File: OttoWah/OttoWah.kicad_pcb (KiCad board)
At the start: 2 copper layers, 38.6 x 34.5 mm, 26 parts, among them J1 Conn_01x02_Female, J2 Conn_01x02_Female, J3 Conn_01x01_Female, J4 Conn_01x01_Female, J5 Conn_01x01_Female, J6 Conn_01x01_Female, U1 TL072, U2 Optocoupler

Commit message: First revision of pedal board - all footprints finalized
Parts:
- moved J4 34.7 mm to (190.2, 55.3)
- moved R3 18.8 mm to (172.8, 65.0), turned to 180 degrees
- moved D1 7.15 mm to (188.0, 37.5)
- moved U2 6.11 mm to (157.5, 34.3)
- moved C1 4.96 mm to (165.1, 60.3), turned to 270 degrees
- moved J1 2.67 mm to (161.3, 64.1), turned to 180 degrees
- moved R8 0.89 mm to (177.8, 42.9)
- moved R5 0.76 mm to (157.5, 43.9)
- moved R1 0.16 mm to (167.7, 60.3)
- moved R2 0.16 mm to (167.7, 62.6)
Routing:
- net Net-(R3-Pad1): track 12.6 -> 51.4 mm
- net Net-(C1-Pad1): track 31.8 -> 22.6 mm
- net Net-(D1-Pad2): track 6.44 -> 11.4 mm
- net Net-(C2-Pad2): track 25.1 -> 29.5 mm
- net Net-(R2-Pad1): track 15.8 -> 16.6 mm
- net Net-(R5-Pad1): track 9.14 -> 8.57 mm
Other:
- net class Default: trace_width 0.25 -> 0.254
- net class Power added: clearance 0.2, trace_width 0.508, via_dia 0.8, via_drill 0.4

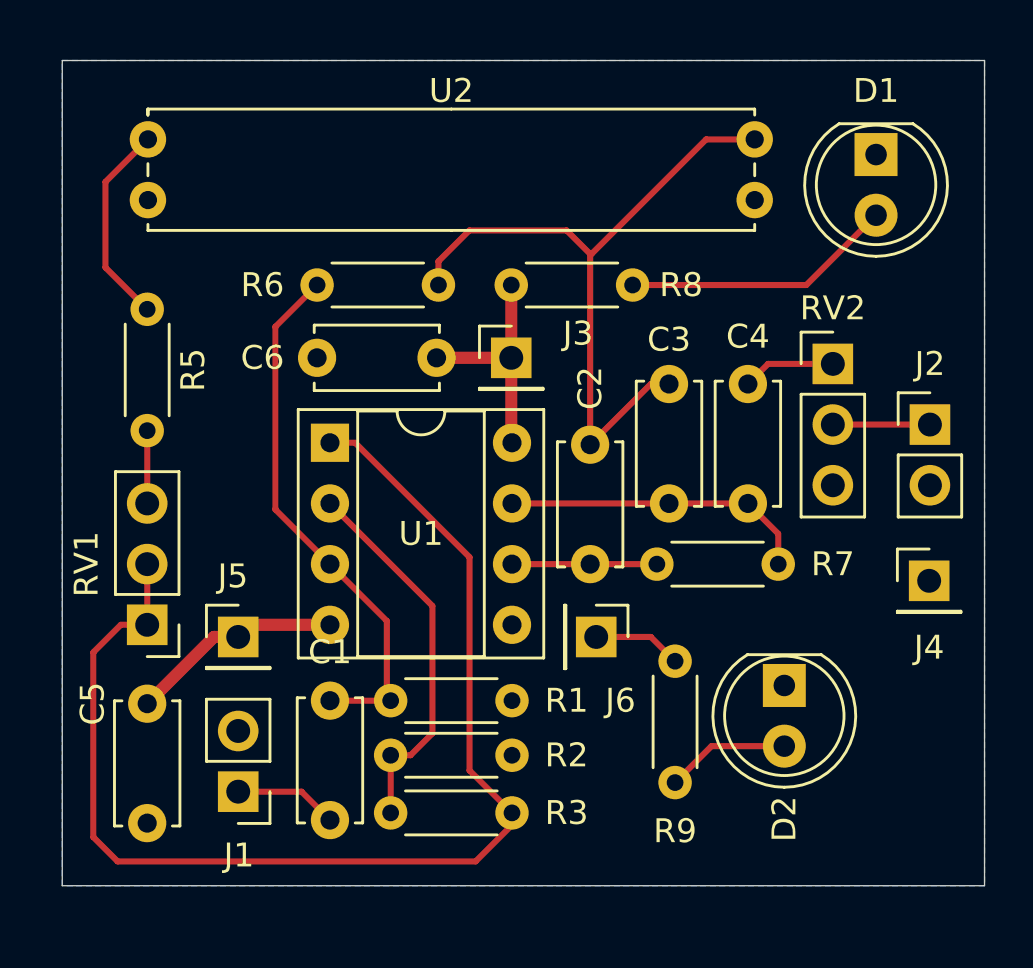
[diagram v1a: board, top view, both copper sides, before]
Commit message: Completely revamped layout and routing, and updated diode footprints. Should be ready for ordering!
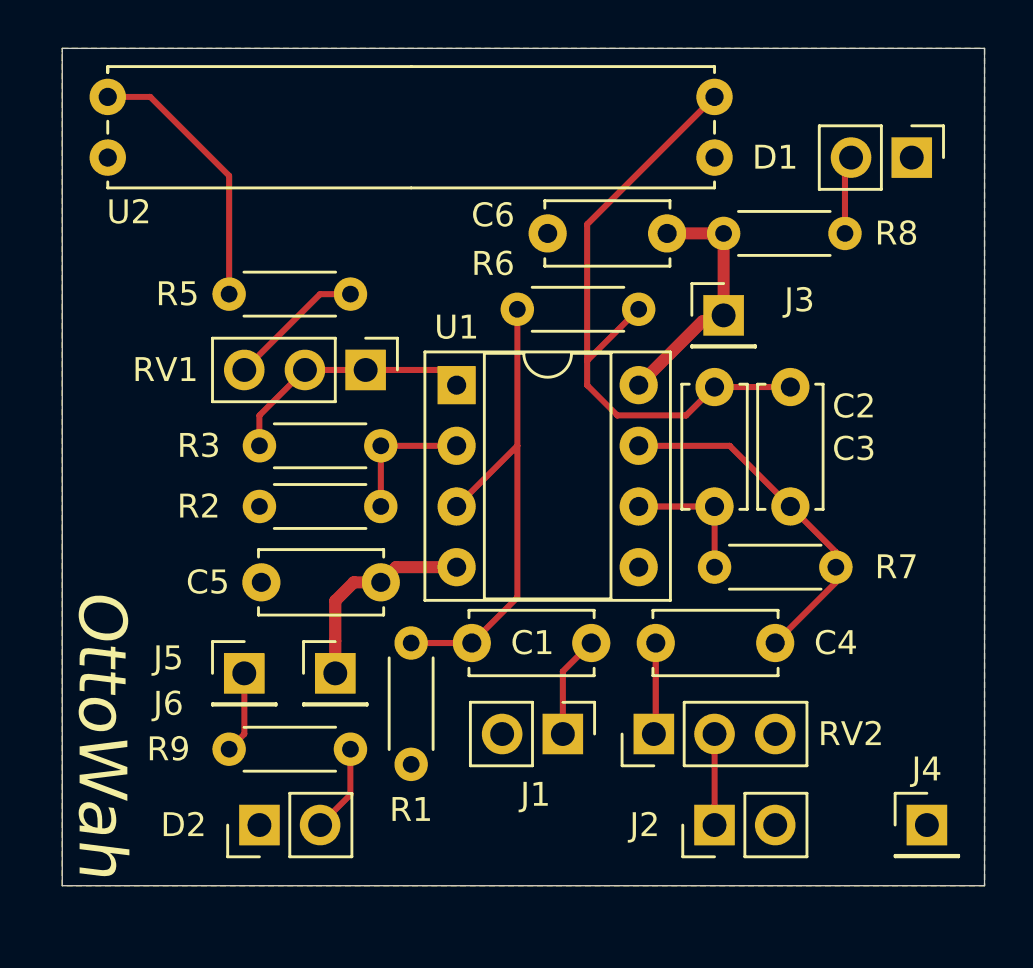
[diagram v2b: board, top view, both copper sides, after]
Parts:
- D1, D2: footprint LED_THT:LED_D5.0mm -> Connector_PinHeader_2.54mm:PinHeader_1x02_P2.54mm_Vertical
- moved D2 22.7 mm to (162.2, 65.5), turned to 90 degrees
- moved J2 19.0 mm to (181.2, 65.5), turned to 90 degrees
- moved R3 18.7 mm to (162.2, 49.7), turned to 0 degrees
- moved RV2 17.2 mm to (178.7, 61.7), turned to 90 degrees
- moved J6 14.8 mm to (161.5, 59.2), turned to 0 degrees
- moved RV1 14.1 mm to (166.6, 46.5), turned to 270 degrees
- moved J1 13.8 mm to (174.9, 61.7), turned to 270 degrees
- moved R9 13.7 mm to (166.0, 62.4), turned to 180 degrees
- moved C5 11.0 mm to (167.3, 55.4), turned to 180 degrees
- moved C6 11.0 mm to (174.2, 40.8)
- moved R2 10.4 mm to (167.3, 52.2), turned to 180 degrees
- moved J4 10.2 mm to (190.1, 65.5)
- moved R8 9.15 mm to (186.7, 40.8)
- moved J3 9.07 mm to (181.6, 44.2)
- moved R6 8.44 mm to (178.1, 43.9)
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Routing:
- net Net-(R3-Pad1): track 51.4 -> 10.6 mm
- net Net-(R2-Pad1): track 16.6 -> 5.72 mm
- net Net-(D1-Pad2): track 11.4 -> 3.28 mm
- net Net-(R5-Pad1): track 8.57 -> 11.4 mm
- net Net-(R5-Pad2): track 3.05 -> 5.76 mm
- net Net-(C2-Pad2): track 29.5 -> 26.9 mm
- net Net-(C3-Pad1): track 12.9 -> 15.0 mm
- net Net-(C1-Pad1): track 22.6 -> 20.9 mm
- net Net-(D2-Pad2): track 5.20 -> 3.70 mm
- net +9V: track 9.74 -> 10.6 mm
- added copper zone on F.Cu, net GND
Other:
- board size 38.6 x 34.5 mm -> 38.6 x 35.1 mm
- board text added: "OttoWah"

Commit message: Ordered version
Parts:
- moved RV2 7.24 mm to (185.7, 59.8), turned to 270 degrees
- moved C4 6.54 mm to (189.5, 54.7), turned to 270 degrees
- moved J2 2.69 mm to (183.1, 63.6), turned to 270 degrees
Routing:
- net Net-(C2-Pad2): track 26.9 -> 28.0 mm
- net Net-(C3-Pad1): track 15.0 -> 13.9 mm
